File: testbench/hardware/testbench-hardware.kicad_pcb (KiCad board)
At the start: 2 copper layers, 88.9 x 88.9 mm, 43 parts, among them J1 ZIF DIP-16 Socket, Q1 ZTX458, SW1 Action, SW2 Mode Select, SW3 Enable Power

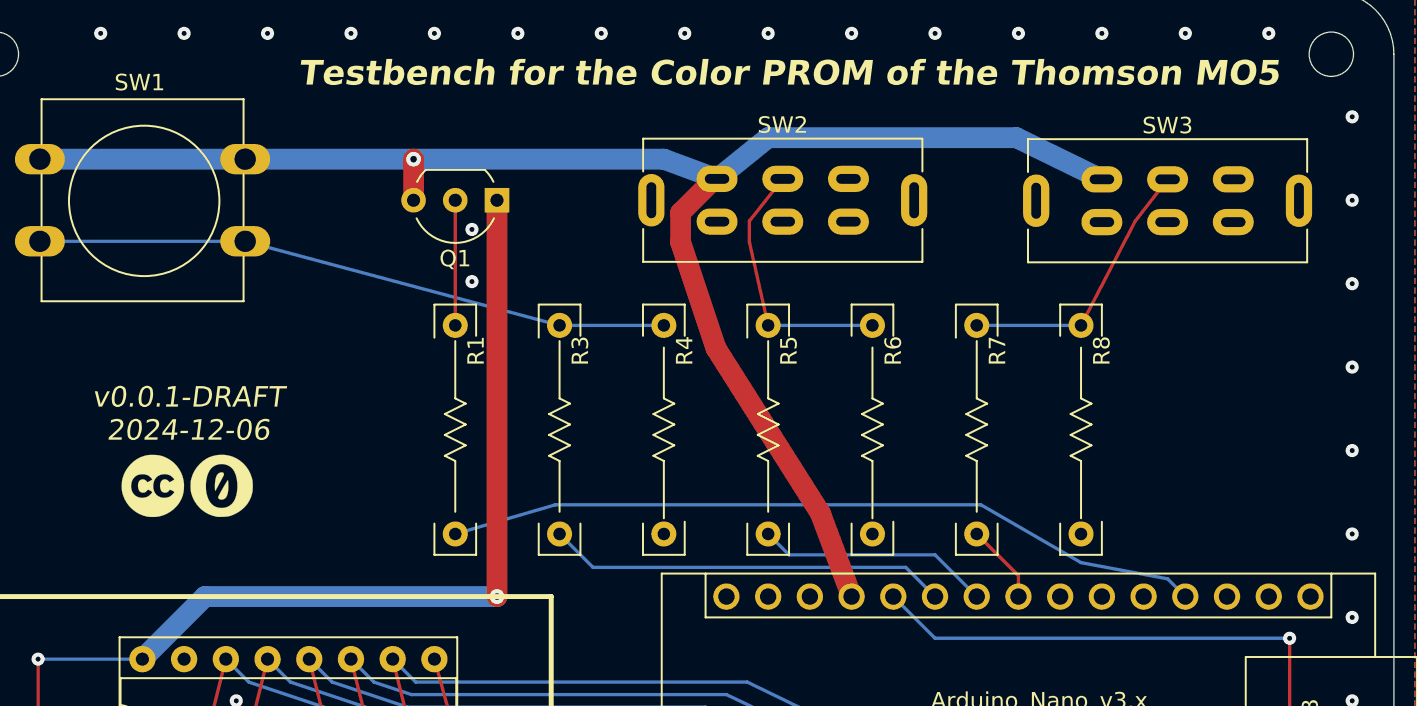
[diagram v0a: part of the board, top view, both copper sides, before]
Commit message: [testbench] uses DPDT switches as SPDT switches for nicer routing
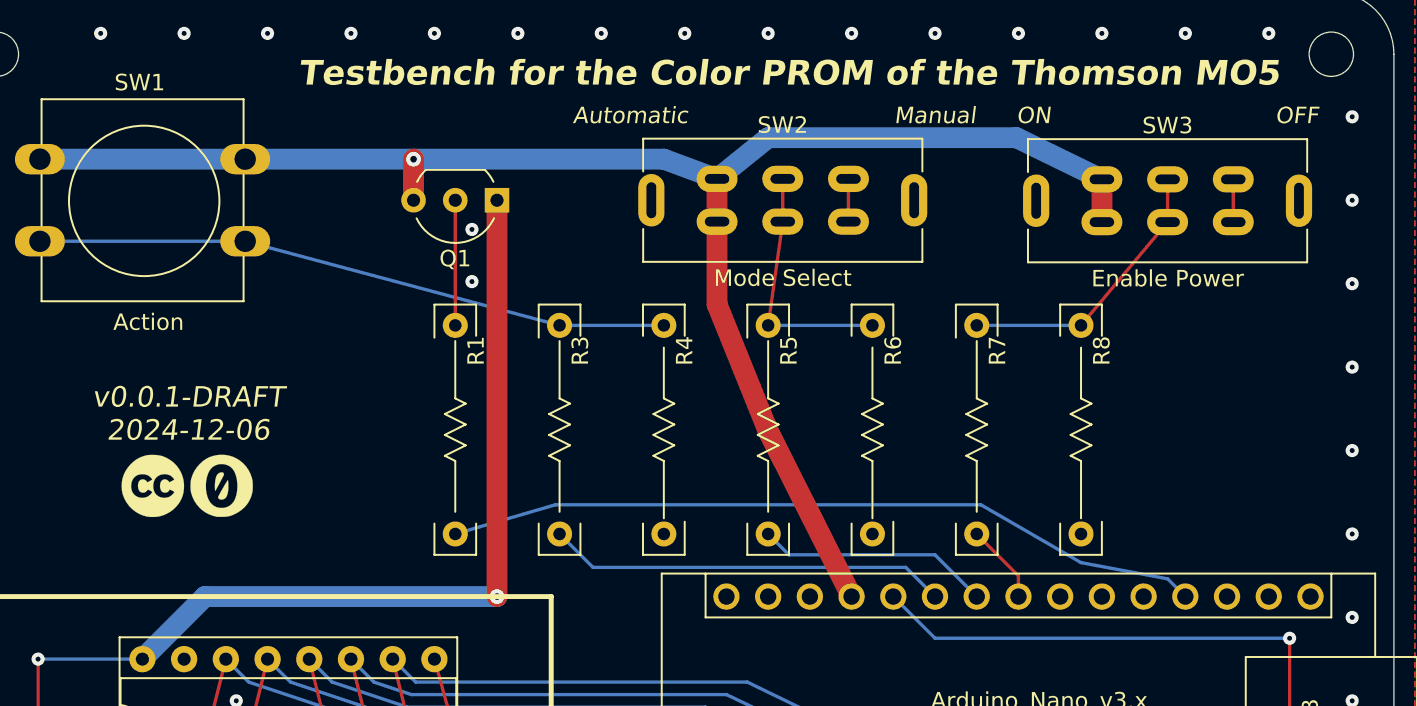
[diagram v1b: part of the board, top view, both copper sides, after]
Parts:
- SW2, SW3: footprint commons-interconnect_THT:g-switch_22f12-gxxx -> commons-interconnect_THT:g-switch_22f12-gxxx--SPDT
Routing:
- net unconnected-(SW3-A-Pad3): track 0.00 -> 2.60 mm
- net unconnected-(SW2-A-Pad3): track 0.00 -> 2.60 mm
- net +5V: track 97.8 -> 98.7 mm
- net Net-(SW2-B): track 16.1 -> 15.3 mm
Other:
- board text added: "Automatic"
- board text added: "Manual"
- board text added: "OFF"
- board text added: "ON"
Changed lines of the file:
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@@
   (setup
     (stackup
-      (layer "F.SilkS" (type "Top Silk Screen"))
+      (layer "F.SilkS" (type "Top Silk Screen") (color "Black"))
       (layer "F.Paste" (type "Top Solder Paste"))
-      (layer "F.Mask" (type "Top Solder Mask") (thickness 0.01))
+      (layer "F.Mask" (type "Top Solder Mask") (color "White") (thickness 0.01))
       (layer "F.Cu" (type "copper") (thickness 0.035))
       (layer "dielectric 1" (type "core") (thickness 1.51) (material "FR4") (epsilon_r 4.5) (loss_tangent 0.02))
       (layer "B.Cu" (type "copper") (thickness 0.035))
-      (layer "B.Mask" (type "Bottom Solder Mask") (thickness 0.01))
+      (layer "B.Mask" (type "Bottom Solder Mask") (color "White") (thickness 0.01))
       (layer "B.Paste" (type "Bottom Solder Paste"))
-      (layer "B.SilkS" (type "Bottom Silk Screen"))
-      (copper_finish "None")
+      (layer "B.SilkS" (type "Bottom Silk Screen") (color "Black"))
+      (copper_finish "HAL lead-free")
       (dielectric_constraints no)
     )
@@
         (effects (font (size 1 1) (thickness 0.15)))
     )
-    (fp_text value "Action" (at 6.62 9.93) (layer "F.Fab")
+    (fp_text value "Action" (at 6.62 9.93) (layer "F.SilkS")
         (effects (font (size 1 1) (thickness 0.15)))
     )
@@
     )
   )
-  (footprint "commons-interconnect_THT:g-switch_22f12-gxxx" (layer "F.Cu")
+  (footprint "commons-interconnect_THT:g-switch_22f12-gxxx--SPDT" (layer "F.Cu")
     (at 115.19 76.2)
-    (descr "DPDT slide switch, https://datasheet.lcsc.com/lcsc/2108301530_G-Switch-SS-22F12-G060_C2848906.pdf")
-    (tags "dpdt, switch, slide")
+    (descr "DPDT slide switch used as SPDT slide switch, https://datasheet.lcsc.com/lcsc/2108301530_G-Switch-SS-22F12-G060_C2848906.pdf")
+    (tags "spdt, switch, slide")
     (property "Sheetfile" "testbench-hardware.kicad_sch")
     (property "Sheetname" "")
@@
         (effects (font (size 1 1) (thickness 0.15)))
     )
-    (fp_text value "Mode Select" (at 0 4.75 unlocked) (layer "F.Fab")
+    (fp_text value "Mode Select" (at 0 4.75 unlocked) (layer "F.SilkS")
         (effects (font (size 1 1) (thickness 0.15)))
     )
@@
     (pad "1" thru_hole oval (at -4 -1.3) (size 2.5 1.6) (drill oval 1.5 0.6) (layers "*.Cu" "*.Mask")
       (net 27 "+5V") (pinfunction "C") (pintype "passive"))
+    (pad "1" thru_hole oval (at -4 1.3) (size 2.5 1.6) (drill oval 1.5 0.6) (layers "*.Cu" "*.Mask")
+      (net 27 "+5V") (pinfunction "C") (pintype "passive"))
     (pad "2" thru_hole oval (at 0 -1.3) (size 2.5 1.6) (drill oval 1.5 0.6) (layers "*.Cu" "*.Mask")
       (net 47 "Net-(SW2-B)") (pinfunction "B") (pintype "passive"))
+    (pad "2" thru_hole oval (at 0 1.3) (size 2.5 1.6) (drill oval 1.5 0.6) (layers "*.Cu" "*.Mask")
+      (net 47 "Net-(SW2-B)") (pinfunction "B") (pintype "passive"))
     (pad "3" thru_hole oval (at 4 -1.3) (size 2.5 1.6) (drill oval 1.5 0.6) (layers "*.Cu" "*.Mask")
       (net 49 "unconnected-(SW2-A-Pad3)") (pinfunction "A") (pintype "passive+no_connect"))
-    (pad "4" thru_hole oval (at -4 1.3) (size 2.5 1.6) (drill oval 1.5 0.6) (layers "*.Cu" "*.Mask"))
-    (pad "5" thru_hole oval (at 0 1.3) (size 2.5 1.6) (drill oval 1.5 0.6) (layers "*.Cu" "*.Mask"))
-    (pad "6" thru_hole oval (at 4 1.3) (size 2.5 1.6) (drill oval 1.5 0.6) (layers "*.Cu" "*.Mask"))
+    (pad "3" thru_hole oval (at 4 1.3) (size 2.5 1.6) (drill oval 1.5 0.6) (layers "*.Cu" "*.Mask")
+      (net 49 "unconnected-(SW2-A-Pad3)") (pinfunction "A") (pintype "passive+no_connect"))
   )
   (footprint "cliparts:logo--cc--zero" (layer "F.Cu")
@@
     )
   )
-  (footprint "commons-interconnect_THT:g-switch_22f12-gxxx" (layer "F.Cu")
+  (footprint "commons-interconnect_THT:g-switch_22f12-gxxx--SPDT" (layer "F.Cu")
     (at 138.62 76.23)
-    (descr "DPDT slide switch, https://datasheet.lcsc.com/lcsc/2108301530_G-Switch-SS-22F12-G060_C2848906.pdf")
-    (tags "dpdt, switch, slide")
+    (descr "DPDT slide switch used as SPDT slide switch, https://datasheet.lcsc.com/lcsc/2108301530_G-Switch-SS-22F12-G060_C2848906.pdf")
+    (tags "spdt, switch, slide")
     (property "Sheetfile" "testbench-hardware.kicad_sch")
     (property "Sheetname" "")
@@
         (effects (font (size 1 1) (thickness 0.15)))
     )
-    (fp_text value "Enable Power" (at 0 4.75 unlocked) (layer "F.Fab")
+    (fp_text value "Enable Power" (at 0 4.75 unlocked) (layer "F.SilkS")
         (effects (font (size 1 1) (thickness 0.15)))
     )
@@
     (pad "1" thru_hole oval (at -4 -1.3) (size 2.5 1.6) (drill oval 1.5 0.6) (layers "*.Cu" "*.Mask")
       (net 27 "+5V") (pinfunction "C") (pintype "passive"))
+    (pad "1" thru_hole oval (at -4 1.3) (size 2.5 1.6) (drill oval 1.5 0.6) (layers "*.Cu" "*.Mask")
+      (net 27 "+5V") (pinfunction "C") (pintype "passive"))
     (pad "2" thru_hole oval (at 0 -1.3) (size 2.5 1.6) (drill oval 1.5 0.6) (layers "*.Cu" "*.Mask")
       (net 48 "Net-(SW3-B)") (pinfunction "B") (pintype "passive"))
+    (pad "2" thru_hole oval (at 0 1.3) (size 2.5 1.6) (drill oval 1.5 0.6) (layers "*.Cu" "*.Mask")
+      (net 48 "Net-(SW3-B)") (pinfunction "B") (pintype "passive"))
     (pad "3" thru_hole oval (at 4 -1.3) (size 2.5 1.6) (drill oval 1.5 0.6) (layers "*.Cu" "*.Mask")
       (net 50 "unconnected-(SW3-A-Pad3)") (pinfunction "A") (pintype "passive+no_connect"))
-    (pad "4" thru_hole oval (at -4 1.3) (size 2.5 1.6) (drill oval 1.5 0.6) (layers "*.Cu" "*.Mask"))
-    (pad "5" thru_hole oval (at 0 1.3) (size 2.5 1.6) (drill oval 1.5 0.6) (layers "*.Cu" "*.Mask"))
-    (pad "6" thru_hole oval (at 4 1.3) (size 2.5 1.6) (drill oval 1.5 0.6) (layers "*.Cu" "*.Mask"))
+    (pad "3" thru_hole oval (at 4 1.3) (size 2.5 1.6) (drill oval 1.5 0.6) (layers "*.Cu" "*.Mask")
+      (net 50 "unconnected-(SW3-A-Pad3)") (pinfunction "A") (pintype "passive+no_connect"))
   )
   (footprint "LED_THT:LED_D3.0mm" (layer "F.Cu")
@@
   (gr_line (start 63.5 67.31) (end 67.31 67.31)
     (stroke (width 0.1) (type default)) (layer "User.2"))
+  (gr_text "ON" (at 129.413 71.628) (layer "F.SilkS")
+    (effects (font (size 1 1) (thickness 0.1) italic) (justify left bottom))
+  )
+  (gr_text "Manual" (at 124.46 71.628) (layer "F.SilkS")
+    (effects (font (size 1 1) (thickness 0.1) italic) (justify bottom))
+  )
   (gr_text "${TITLE}" (at 115.57 69.342) (layer "F.SilkS")
     (effects (font (size 1.5 1.5) (thickness 0.3) bold italic) (justify bottom))
   )
+  (gr_text "Automatic" (at 105.918 71.628) (layer "F.SilkS")
+    (effects (font (size 1 1) (thickness 0.1) italic) (justify bottom))
+  )
   (gr_text "${REVISION}\n${ISSUE_DATE}" (at 78.994 90.932) (layer "F.SilkS")
     (effects (font (size 1.25 1.25) (thickness 0.15625) italic) (justify bottom))
   )
+  (gr_text "OFF" (at 147.828 71.628) (layer "F.SilkS")
+    (effects (font (size 1 1) (thickness 0.1) italic) (justify right bottom))
+  )
   (via (at 124.46 66.04) (size 0.8) (drill 0.3) (layers "F.Cu" "B.Cu") (free) (net 4))
   (via (at 66.04 106.68) (size 0.8) (drill 0.3) (layers "F.Cu" "B.Cu") (free) (net 4))
@@
   (segment (start 113.03 127) (end 114.3 128.27) (width 0.2) (layer "B.Cu") (net 26))
   (segment (start 104.14 124.968) (end 96.52 118.11) (width 0.2) (layer "B.Cu") (net 26))
-  (segment (start 111.125 85.217) (end 108.966 78.74) (width 1.27) (layer "F.Cu") (net 27))
-  (segment (start 117.475 95.25) (end 119.38 100.33) (width 1.27) (layer "F.Cu") (net 27))
-  (segment (start 108.966 76.961761) (end 108.966 78.74) (width 1.27) (layer "F.Cu") (net 27))
-  (segment (start 111.19 74.9) (end 111.027761 74.9) (width 1.27) (layer "F.Cu") (net 27))
+  (segment (start 111.19 77.5) (end 111.19 82.55) (width 1.27) (layer "F.Cu") (net 27))
+  (segment (start 134.62 77.53) (end 134.62 74.93) (width 1.27) (layer "F.Cu") (net 27))
+  (segment (start 114.275388 90.194612) (end 111.19 82.55) (width 1.27) (layer "F.Cu") (net 27))
+  (segment (start 111.19 74.9) (end 111.19 77.5) (width 1.27) (layer "F.Cu") (net 27))
   (segment (start 92.71 76.2) (end 92.71 73.7) (width 1.27) (layer "F.Cu") (net 27))
-  (segment (start 111.027761 74.9) (end 108.966 76.961761) (width 1.27) (layer "F.Cu") (net 27))
-  (segment (start 117.475 95.25) (end 111.125 85.217) (width 1.27) (layer "F.Cu") (net 27))
+  (segment (start 114.275388 90.194612) (end 119.38 100.33) (width 1.27) (layer "F.Cu") (net 27))
   (via (at 92.71 73.7) (size 0.9) (drill 0.4) (layers "F.Cu" "B.Cu") (net 27))
   (segment (start 129.413 72.39) (end 114.3 72.39) (width 1.27) (layer "B.Cu") (net 27))
@@
   (segment (start 82.46 78.7) (end 101.6 83.82) (width 0.2) (layer "B.Cu") (net 46))
   (segment (start 101.6 83.82) (end 107.95 83.82) (width 0.2) (layer "B.Cu") (net 46))
-  (segment (start 113.157 78.74) (end 114.3 83.82) (width 0.2) (layer "F.Cu") (net 47))
-  (segment (start 113.157 78.74) (end 113.157 77.47) (width 0.2) (layer "F.Cu") (net 47))
-  (segment (start 115.19 74.9) (end 113.157 77.47) (width 0.2) (layer "F.Cu") (net 47))
+  (segment (start 115.19 74.9) (end 115.19 77.5) (width 0.2) (layer "F.Cu") (net 47))
+  (segment (start 114.3 83.82) (end 115.19 77.5) (width 0.2) (layer "F.Cu") (net 47))
   (segment (start 114.3 83.82) (end 120.65 83.82) (width 0.2) (layer "B.Cu") (net 47))
-  (segment (start 136.652 77.47) (end 138.62 74.93) (width 0.2) (layer "F.Cu") (net 48))
-  (segment (start 136.652 77.47) (end 133.35 83.82) (width 0.2) (layer "F.Cu") (net 48))
+  (segment (start 138.62 74.93) (end 138.62 77.53) (width 0.2) (layer "F.Cu") (net 48))
+  (segment (start 133.35 83.82) (end 138.62 77.53) (width 0.2) (layer "F.Cu") (net 48))
   (segment (start 127 83.82) (end 133.35 83.82) (width 0.2) (layer "B.Cu") (net 48))
+  (segment (start 119.19 77.5) (end 119.19 74.9) (width 0.2) (layer "F.Cu") (net 49))
+  (segment (start 142.62 74.93) (end 142.62 77.53) (width 0.2) (layer "F.Cu") (net 50))
   (zone (net 4) (net_name "GND") (layers "F&B.Cu") (hatch edge 0.5)
     (connect_pads (clearance 0.5))

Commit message: Fixes #2 : [bug][testbench][hardware] A6 and A7 cannot be used as digital input
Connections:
- net Net-(A1-A4) renamed /POWER_ENABLE_SWITCH
- net Net-(A1-A5) renamed /MODE_SWITCH
- A1 pad 20: unconnected-(A1-A1-Pad20) -> /R0
- A1 pad 21: unconnected-(A1-A2-Pad21) -> /ACTION_BUTTON
- A1 pad 25: Net-(A1-A6) -> unconnected-(A1-A6-Pad25)
- A1 pad 26: /R0 -> unconnected-(A1-A7-Pad26)
- R3 pad 2: Net-(A1-A6) -> /ACTION_BUTTON
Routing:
- net /ACTION_BUTTON: track 0.00 -> 35.8 mm
- net Net-(A1-A6): track 24.4 -> 0.00 mm
- net /R0: track 125.7 -> 110.5 mm
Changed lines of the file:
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@@
   (net 18 "unconnected-(A1-AREF-Pad18)")
   (net 19 "Net-(A1-A0)")
-  (net 20 "unconnected-(A1-A1-Pad20)")
-  (net 21 "unconnected-(A1-A2-Pad21)")
+  (net 20 "/ACTION_BUTTON")
+  (net 21 "/POWER_ENABLE_SWITCH")
   (net 22 "unconnected-(A1-A3-Pad22)")
-  (net 23 "Net-(A1-A4)")
-  (net 24 "Net-(A1-A5)")
-  (net 25 "Net-(A1-A6)")
+  (net 23 "/MODE_SWITCH")
+  (net 24 "unconnected-(A1-A6-Pad25)")
+  (net 25 "unconnected-(A1-A7-Pad26)")
   (net 26 "/B1")
   (net 27 "+5V")
@@
       (net 46 "Net-(R3-Pad1)") (pintype "passive"))
     (pad "2" thru_hole circle (at 6.35 0 270) (size 1.524 1.524) (drill 0.762) (layers "*.Cu" "*.Mask")
-      (net 25 "Net-(A1-A6)") (pintype "passive"))
+      (net 20 "/ACTION_BUTTON") (pintype "passive"))
     (model "${KISYS3DMOD}/Resistor_THT.3dshapes/R_Axial_DIN0207_L6.3mm_D2.5mm_P15.24mm_Horizontal.wrl"
       (offset (xyz -6 0 0))
@@
       (net 47 "Net-(SW2-B)") (pintype "passive"))
     (pad "2" thru_hole circle (at 6.35 0 270) (size 1.524 1.524) (drill 0.762) (layers "*.Cu" "*.Mask")
-      (net 24 "Net-(A1-A5)") (pintype "passive"))
+      (net 23 "/MODE_SWITCH") (pintype "passive"))
     (model "${KISYS3DMOD}/Resistor_THT.3dshapes/R_Axial_DIN0207_L6.3mm_D2.5mm_P15.24mm_Horizontal.wrl"
       (offset (xyz -6 0 0))
@@
       (net 48 "Net-(SW3-B)") (pintype "passive"))
     (pad "2" thru_hole circle (at 6.35 0 270) (size 1.524 1.524) (drill 0.762) (layers "*.Cu" "*.Mask")
-      (net 23 "Net-(A1-A4)") (pintype "passive"))
+      (net 21 "/POWER_ENABLE_SWITCH") (pintype "passive"))
     (model "${KISYS3DMOD}/Resistor_THT.3dshapes/R_Axial_DIN0207_L6.3mm_D2.5mm_P15.24mm_Horizontal.wrl"
       (offset (xyz -6 0 0))
@@
       (net 19 "Net-(A1-A0)") (pinfunction "A0") (pintype "bidirectional"))
     (pad "20" thru_hole oval (at 15.24 25.4 90) (size 1.6 1.6) (drill 1) (layers "*.Cu" "*.Mask")
-      (net 20 "unconnected-(A1-A1-Pad20)") (pinfunction "A1") (pintype "bidirectional+no_connect"))
+      (net 11 "/R0") (pinfunction "A1") (pintype "bidirectional"))
     (pad "21" thru_hole oval (at 15.24 22.86 90) (size 1.6 1.6) (drill 1) (layers "*.Cu" "*.Mask")
-      (net 21 "unconnected-(A1-A2-Pad21)") (pinfunction "A2") (pintype "bidirectional+no_connect"))
+      (net 20 "/ACTION_BUTTON") (pinfunction "A2") (pintype "bidirectional"))
     (pad "22" thru_hole oval (at 15.24 20.32 90) (size 1.6 1.6) (drill 1) (layers "*.Cu" "*.Mask")
       (net 22 "unconnected-(A1-A3-Pad22)") (pinfunction "A3") (pintype "bidirectional+no_connect"))
     (pad "23" thru_hole oval (at 15.24 17.78 90) (size 1.6 1.6) (drill 1) (layers "*.Cu" "*.Mask")
-      (net 23 "Net-(A1-A4)") (pinfunction "A4") (pintype "bidirectional"))
+      (net 21 "/POWER_ENABLE_SWITCH") (pinfunction "A4") (pintype "bidirectional"))
     (pad "24" thru_hole oval (at 15.24 15.24 90) (size 1.6 1.6) (drill 1) (layers "*.Cu" "*.Mask")
-      (net 24 "Net-(A1-A5)") (pinfunction "A5") (pintype "bidirectional"))
+      (net 23 "/MODE_SWITCH") (pinfunction "A5") (pintype "bidirectional"))
     (pad "25" thru_hole oval (at 15.24 12.7 90) (size 1.6 1.6) (drill 1) (layers "*.Cu" "*.Mask")
-      (net 25 "Net-(A1-A6)") (pinfunction "A6") (pintype "bidirectional"))
+      (net 24 "unconnected-(A1-A6-Pad25)") (pinfunction "A6") (pintype "bidirectional+no_connect"))
     (pad "26" thru_hole oval (at 15.24 10.16 90) (size 1.6 1.6) (drill 1) (layers "*.Cu" "*.Mask")
-      (net 11 "/R0") (pinfunction "A7") (pintype "bidirectional"))
+      (net 25 "unconnected-(A1-A7-Pad26)") (pinfunction "A7") (pintype "bidirectional+no_connect"))
     (pad "27" thru_hole oval (at 15.24 7.62 90) (size 1.6 1.6) (drill 1) (layers "*.Cu" "*.Mask")
       (net 27 "+5V") (pinfunction "+5V") (pintype "power_out"))
@@
   (via (at 76.2 114.3) (size 0.8) (drill 0.3) (layers "F.Cu" "B.Cu") (net 11))
   (via (at 146.05 102.87) (size 0.8) (drill 0.3) (layers "F.Cu" "B.Cu") (net 11))
-  (segment (start 124.46 102.87) (end 121.92 100.33) (width 0.2) (layer "B.Cu") (net 11))
+  (segment (start 137.16 100.33) (end 139.7 102.87) (width 0.2) (layer "B.Cu") (net 11))
   (segment (start 76.2 114.3) (end 97.79 114.3) (width 0.2) (layer "B.Cu") (net 11))
+  (segment (start 139.7 102.87) (end 140.8 102.87) (width 0.2) (layer "B.Cu") (net 11))
   (segment (start 144.78 127) (end 146.05 128.27) (width 0.2) (layer "B.Cu") (net 11))
   (segment (start 110.49 121.158) (end 97.79 114.3) (width 0.2) (layer "B.Cu") (net 11))
-  (segment (start 146.05 102.87) (end 124.46 102.87) (width 0.2) (layer "B.Cu") (net 11))
+  (segment (start 146.05 102.87) (end 140.8 102.87) (width 0.2) (layer "B.Cu") (net 11))
   (segment (start 144.78 127) (end 110.49 121.158) (width 0.2) (layer "B.Cu") (net 11))
   (segment (start 139.7 128.27) (end 139.7 121.92) (width 0.2) (layer "F.Cu") (net 12))
@@
   (segment (start 101.346 94.742) (end 127.254 94.742) (width 0.2) (layer "B.Cu") (net 19))
   (segment (start 127.254 94.742) (end 133.35 98.263676) (width 0.2) (layer "B.Cu") (net 19))
-  (segment (start 129.54 100.33) (end 129.54 99.06) (width 0.2) (layer "F.Cu") (net 23))
-  (segment (start 129.54 99.06) (end 127 96.52) (width 0.2) (layer "F.Cu") (net 23))
-  (segment (start 114.3 96.52) (end 115.57 97.79) (width 0.2) (layer "B.Cu") (net 24))
-  (segment (start 115.57 97.79) (end 124.46 97.79) (width 0.2) (layer "B.Cu") (net 24))
-  (segment (start 124.46 97.79) (end 127 100.33) (width 0.2) (layer "B.Cu") (net 24))
-  (segment (start 122.682 98.552) (end 103.632 98.552) (width 0.2) (layer "B.Cu") (net 25))
-  (segment (start 124.46 100.33) (end 122.682 98.552) (width 0.2) (layer "B.Cu") (net 25))
-  (segment (start 103.632 98.552) (end 101.6 96.52) (width 0.2) (layer "B.Cu") (net 25))
+  (segment (start 134.62 100.33) (end 132.334 102.616) (width 0.2) (layer "B.Cu") (net 20))
+  (segment (start 101.6 96.52) (end 110.998 102.616) (width 0.2) (layer "B.Cu") (net 20))
+  (segment (start 132.334 102.616) (end 110.998 102.616) (width 0.2) (layer "B.Cu") (net 20))
+  (segment (start 129.54 100.33) (end 129.54 99.06) (width 0.2) (layer "F.Cu") (net 21))
+  (segment (start 129.54 99.06) (end 127 96.52) (width 0.2) (layer "F.Cu") (net 21))
+  (segment (start 114.3 96.52) (end 115.57 97.79) (width 0.2) (layer "B.Cu") (net 23))
+  (segment (start 115.57 97.79) (end 124.46 97.79) (width 0.2) (layer "B.Cu") (net 23))
+  (segment (start 124.46 97.79) (end 127 100.33) (width 0.2) (layer "B.Cu") (net 23))
   (segment (start 88.9 111.76) (end 88.9 118.11) (width 0.2) (layer "F.Cu") (net 26))
   (segment (start 114.3 128.27) (end 114.3 118.872) (width 0.2) (layer "F.Cu") (net 26))
